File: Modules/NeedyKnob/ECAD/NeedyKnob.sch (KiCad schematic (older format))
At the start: 24 parts, among them J1 comm_header, J2 prog_header, SW1 Knob, U1 ATmega328-PU, U2 MAX7219, U3 LTD6640E

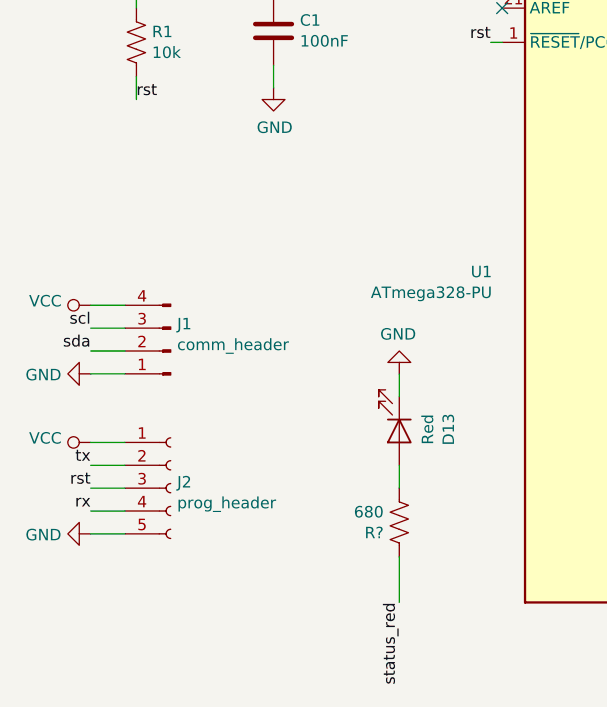
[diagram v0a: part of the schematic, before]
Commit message: Added polyfuses to all modules
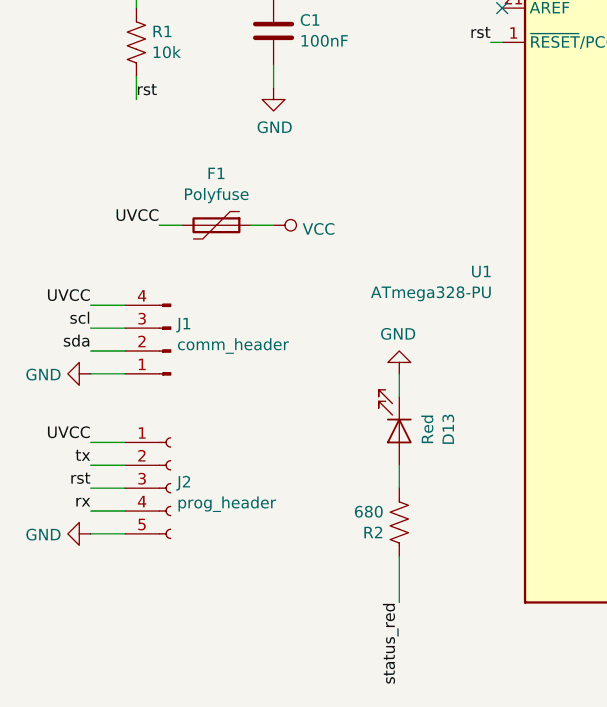
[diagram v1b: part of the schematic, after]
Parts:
- added F1: Polyfuse, symbol Device:Polyfuse
- gave numbers to parts that had none: 1
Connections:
- net VCC: now also F1.1; no longer J1.4 (Pin_4), J2.1 (Pin_1)
- new net UVCC: F1.2, J1.4 (Pin_4), J2.1 (Pin_1)
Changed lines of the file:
@@
 L power:VCC #PWR01
 U 1 1 5F5DC5B2
-P 1400 3350
-F 0 "#PWR01" H 1400 3200 50  0001 C CNN
-F 1 "VCC" V 1418 3477 50  0000 L CNN
-F 2 "" H 1400 3350 50  0001 C CNN
-F 3 "" H 1400 3350 50  0001 C CNN
-	1    1400 3350
-	0    -1   -1   0
-$EndComp
-$Comp
-L power:VCC #PWR03
-U 1 1 5F5DD568
-P 1400 3950
-F 0 "#PWR03" H 1400 3800 50  0001 C CNN
-F 1 "VCC" V 1418 4077 50  0000 L CNN
-F 2 "" H 1400 3950 50  0001 C CNN
-F 3 "" H 1400 3950 50  0001 C CNN
-	1    1400 3950
-	0    -1   -1   0
+P 2200 3000
+F 0 "#PWR01" H 2200 2850 50  0001 C CNN
+F 1 "VCC" V 2218 3127 50  0000 L CNN
+F 2 "" H 2200 3000 50  0001 C CNN
+F 3 "" H 2200 3000 50  0001 C CNN
+	1    2200 3000
+	0    1    1    0
 $EndComp
 $Comp
@@
 NoConn ~ 4400 4350
 $Comp
-L Device:R_US R?
+L Device:R_US R2
 U 1 1 5F65BF8C
 P 2750 4300
-F 0 "R?" H 2818 4346 50  0000 L CNN
+F 0 "R2" H 2818 4346 50  0000 L CNN
 F 1 "680" H 2818 4255 50  0000 L CNN
 F 2 "" V 2790 4290 50  0001 C CNN
@@
 Wire Wire Line
 	2750 4150 2750 4050
+$Comp
+L Device:Polyfuse F1
+U 1 1 5F92424B
+P 1950 3000
+F 0 "F1" V 1725 3000 50  0000 C CNN
+F 1 "Polyfuse" V 1816 3000 50  0000 C CNN
+F 2 "" H 2000 2800 50  0001 L CNN
+F 3 "~" H 1950 3000 50  0001 C CNN
+	1    1950 3000
+	0    1    1    0
+$EndComp
+Text Label 1400 3950 2    50   ~ 0
+UVCC
+Text Label 1400 3350 2    50   ~ 0
+UVCC
+Text Label 1700 3000 2    50   ~ 0
+UVCC
+Wire Wire Line
+	1700 3000 1800 3000
+Wire Wire Line
+	2100 3000 2200 3000
 $EndSCHEMATC
